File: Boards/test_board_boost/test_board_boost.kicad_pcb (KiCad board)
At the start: 4 copper layers, 90 x 75 mm, 101 parts, among them J10 TD, J11 PT, J12 V+RS485, J13 AVR-PDI-6, J14 UART, J15 RS485, J9 TU, U1 MIC2619, U2 MIC2619, U3 LM258DT, U4 MPQ8112GJ, U5 MPQ8112GJ, U6 LM3671MF-3.3/NOPB, U7 ATxmega256A3U-A

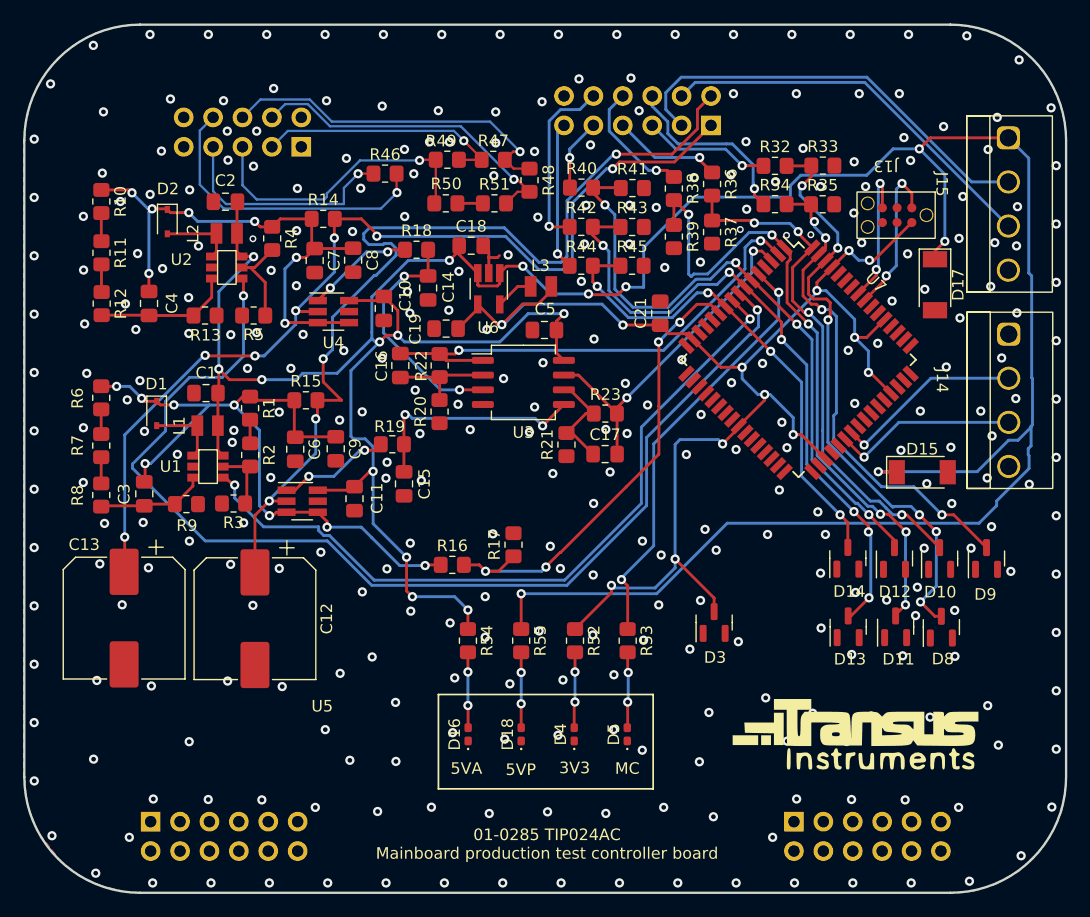
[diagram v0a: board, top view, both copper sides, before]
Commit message: added relay
Still needs better separation between the AC lines and footprints relay need fixing
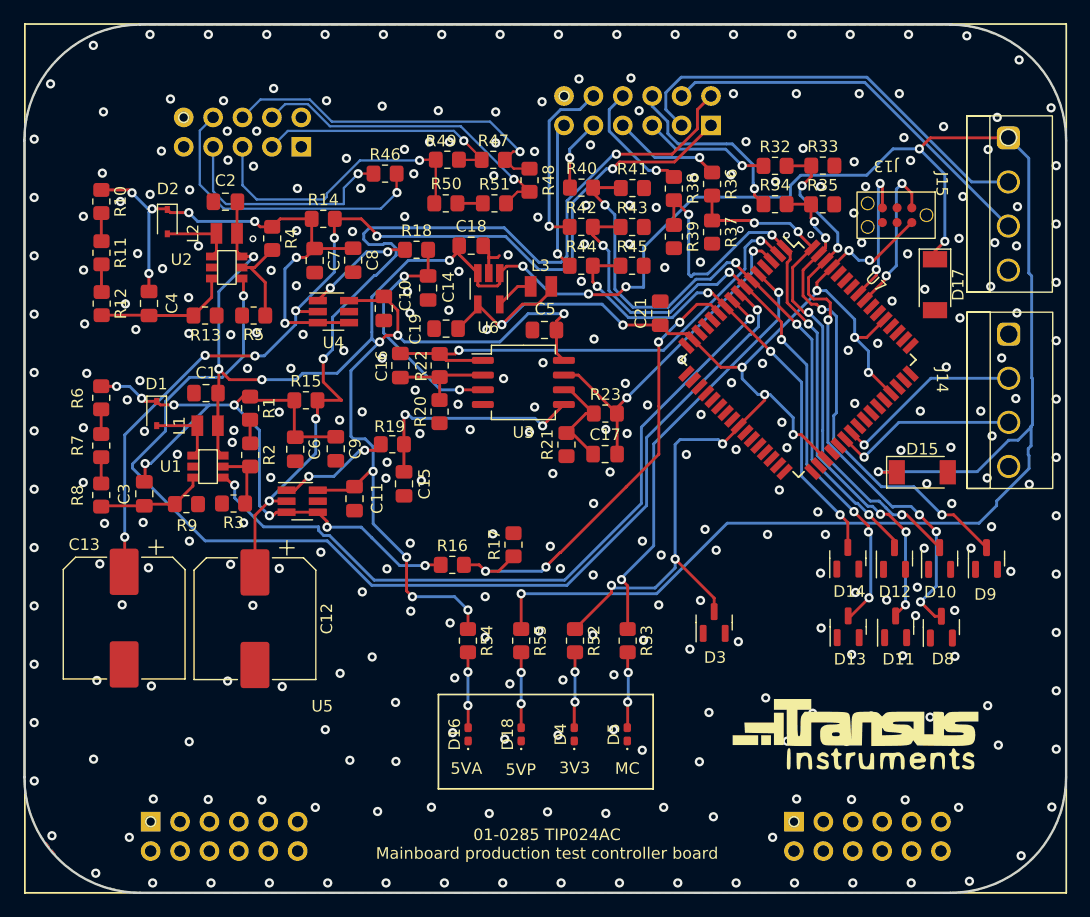
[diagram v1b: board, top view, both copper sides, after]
